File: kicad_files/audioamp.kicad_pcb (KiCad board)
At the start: 2 copper layers, 114.8 x 59.9 mm, 49 parts, among them J1 Conn_01x03_Female, J2 Conn_01x02_Female, U1 TDA2030, U2 TDA2030, U3 TL084

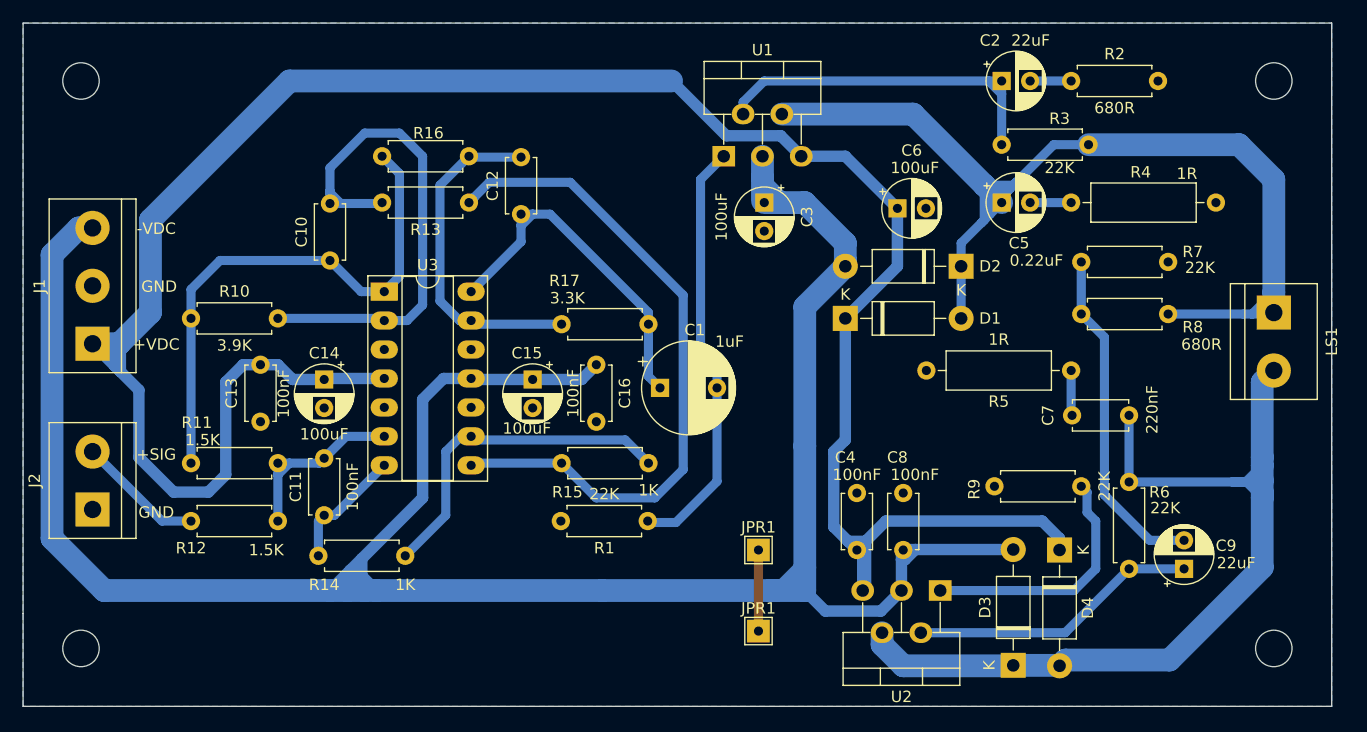
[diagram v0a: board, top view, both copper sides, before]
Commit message: Trilhas engrossadas
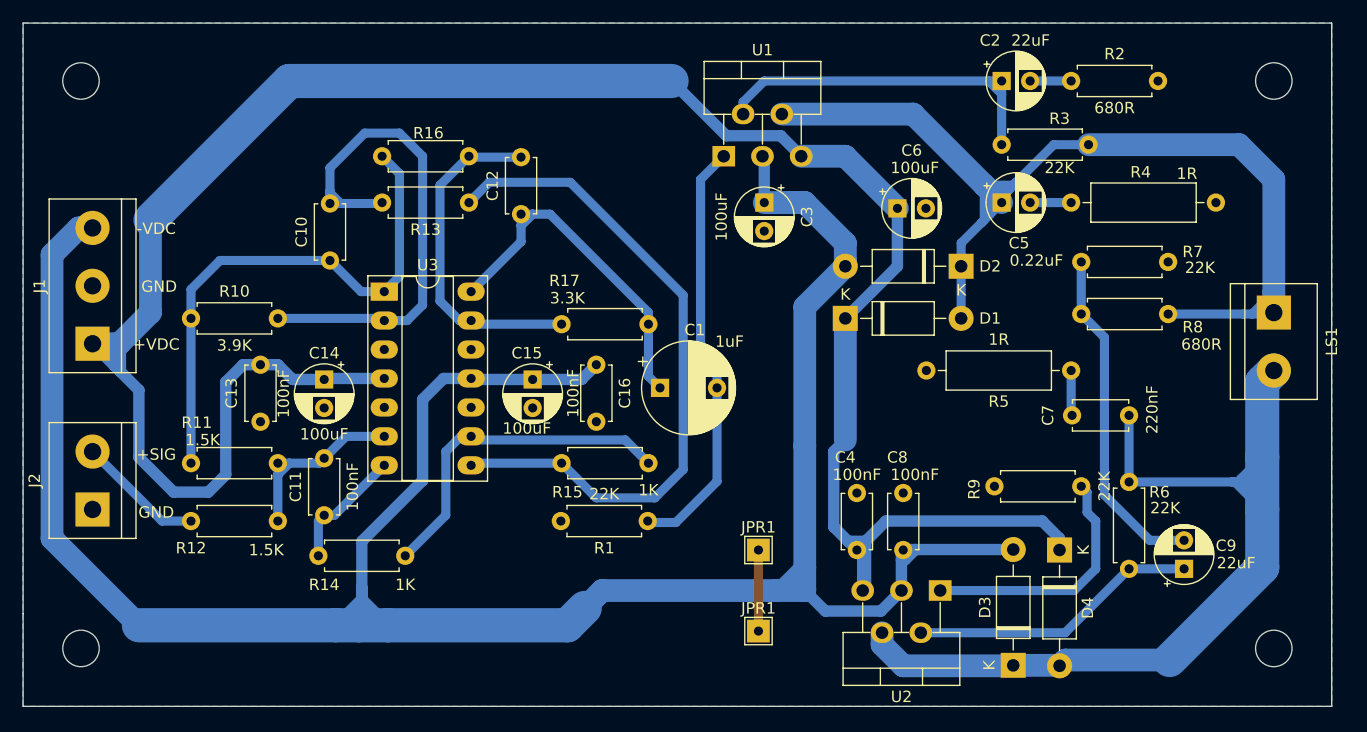
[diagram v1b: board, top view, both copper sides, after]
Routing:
- net -VDC: track 218.6 -> 223.2 mm
- net /OUT-: track 82.3 -> 81.2 mm

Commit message: Pads mais grossos para facilitar solda
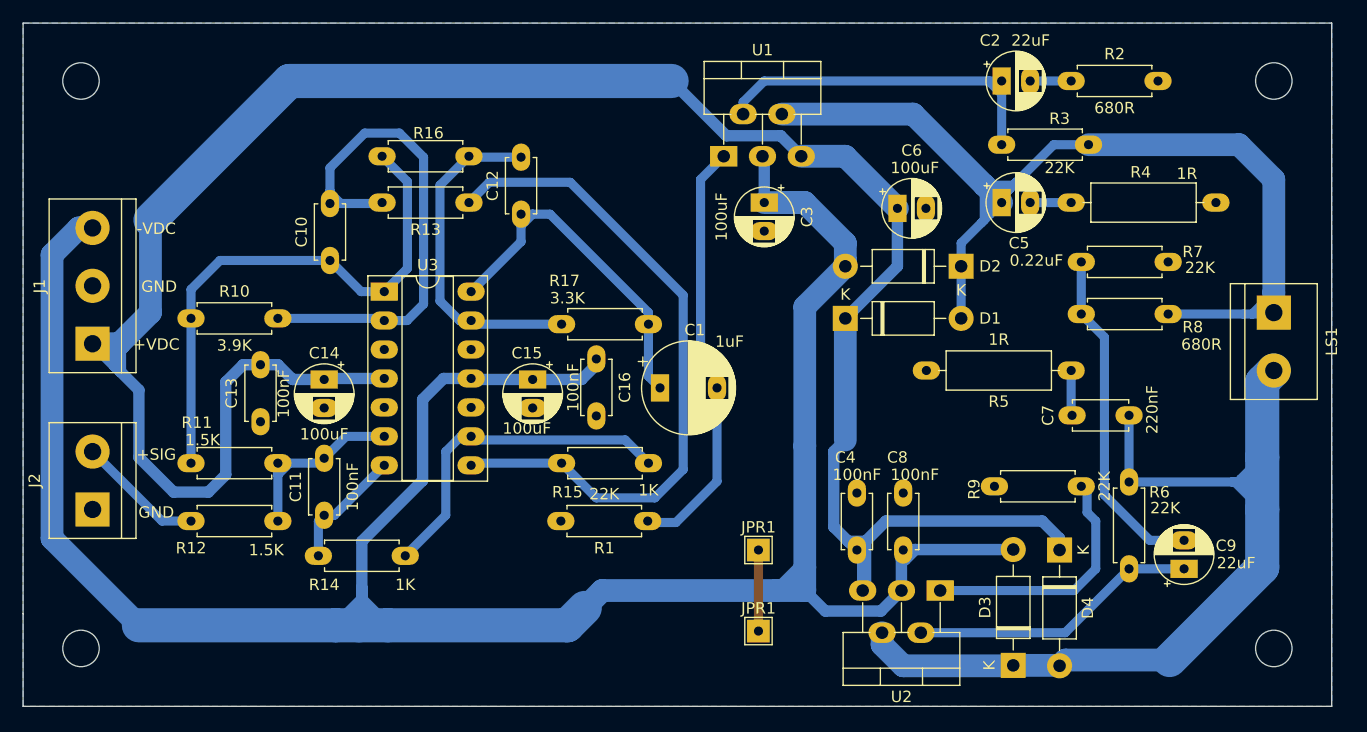
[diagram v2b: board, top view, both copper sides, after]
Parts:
- moved C16 0.51 mm to (96.5, 81.3)
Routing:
- net /Filtro Passa-Baixas/Vo1: track 47.4 -> 48.0 mm
